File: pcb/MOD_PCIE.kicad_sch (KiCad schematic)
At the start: 8 parts, among them J7 2041262-1, SW2 SW_DIP_x01

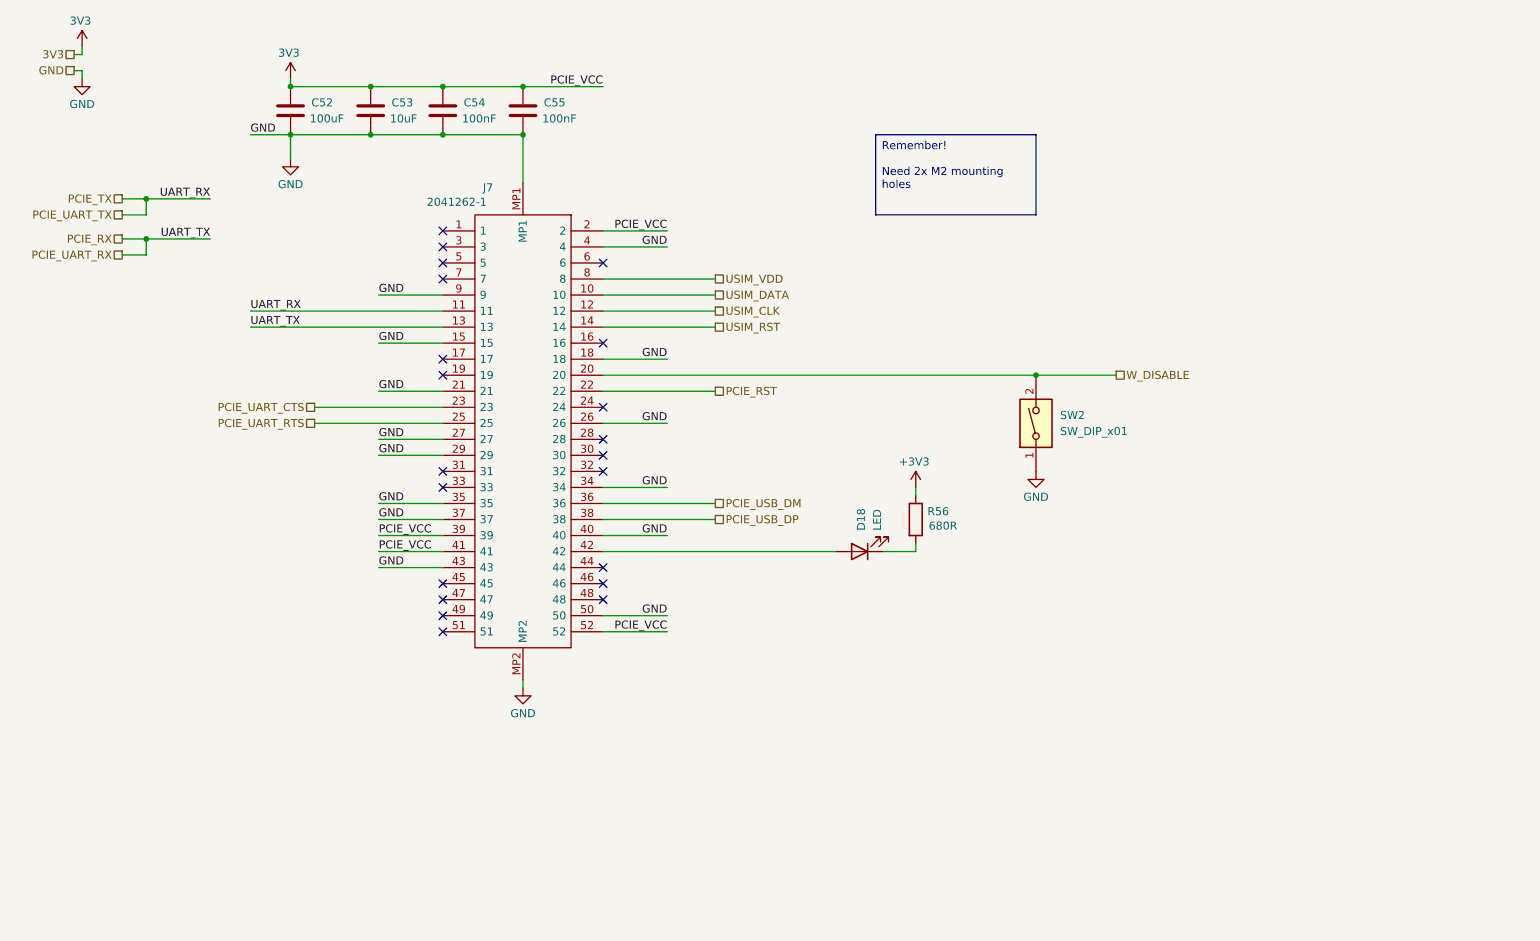
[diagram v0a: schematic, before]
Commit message: updated pcie sd and sim cards
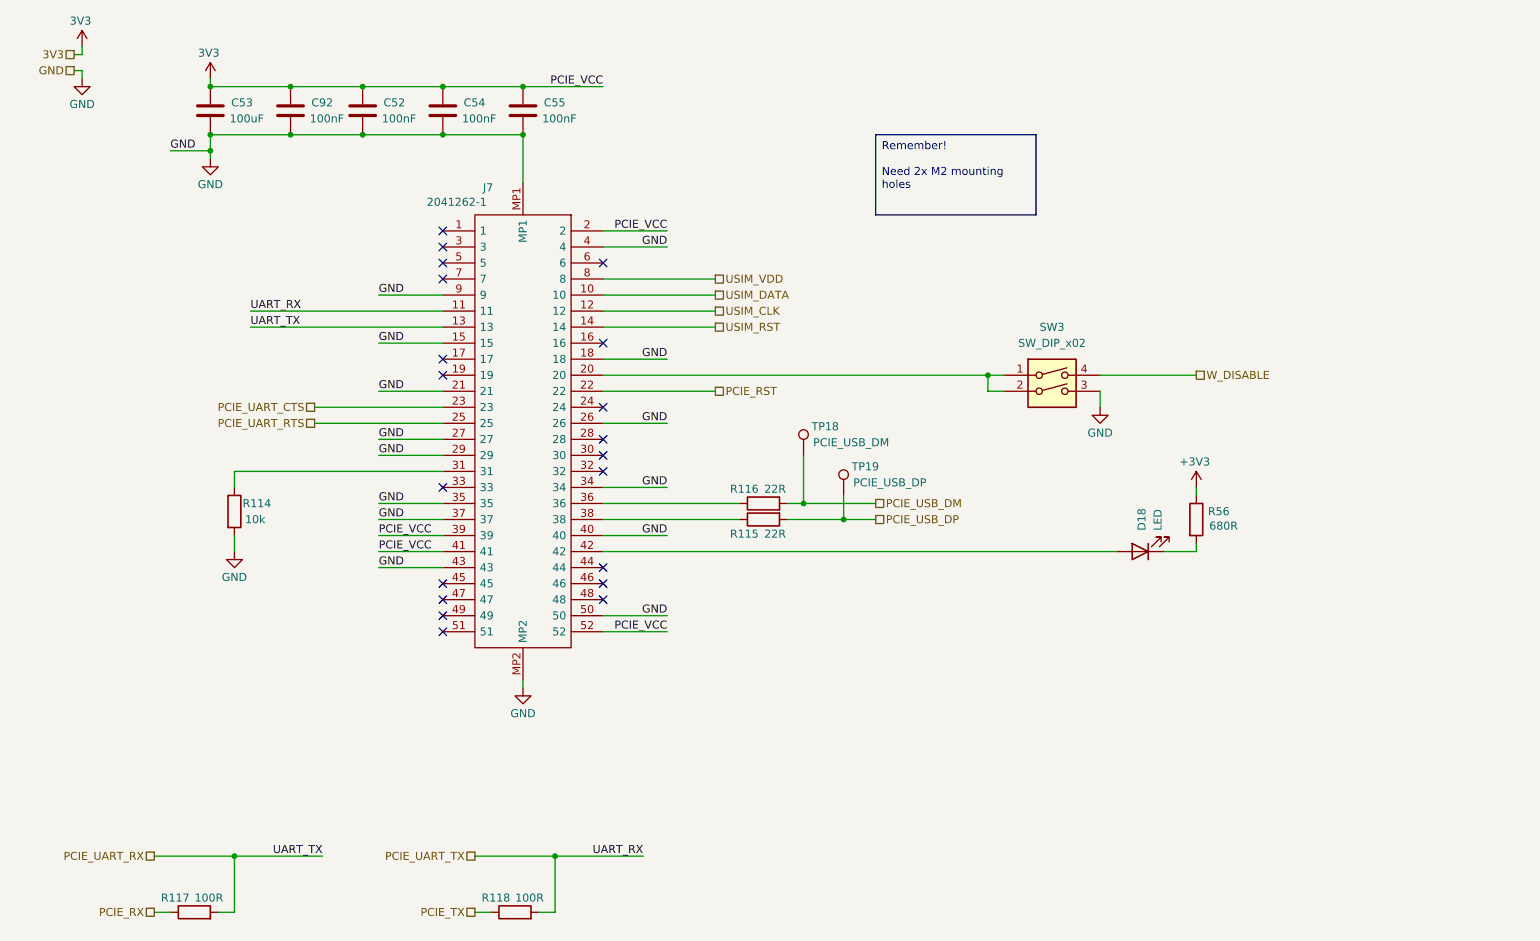
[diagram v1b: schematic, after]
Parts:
- removed SW2: SW_DIP_x01, SamacSys_Parts:DS01254L01BE, symbol Switch:SW_DIP_x01
- added C92: 100nF, Capacitor_SMD:C_0603_1608Metric_Pad1.08x0.95mm_HandSolder, symbol Device:C
- added R114: 10k, Resistor_SMD:R_0603_1608Metric_Pad0.98x0.95mm_HandSolder, symbol Device:R
- added R115, R116: 22R, Resistor_SMD:R_0603_1608Metric_Pad0.98x0.95mm_HandSolder, symbol Device:R
- added R117, R118: 100R, Resistor_SMD:R_0603_1608Metric_Pad0.98x0.95mm_HandSolder, symbol Device:R
- added SW3: SW_DIP_x02, symbol Switch:SW_DIP_x02
- added TP18: PCIE_USB_DM, TestPoint:TestPoint_THTPad_D2.0mm_Drill1.0mm, symbol Connector:TestPoint
- added TP19: PCIE_USB_DP, TestPoint:TestPoint_THTPad_D2.0mm_Drill1.0mm, symbol Connector:TestPoint
- C52: value 100uF -> 100nF; footprint Capacitor_SMD:C_1210_3225Metric_Pad1.33x2.70mm_HandSolder -> Capacitor_SMD:C_0603_1608Metric_Pad1.08x0.95mm_HandSolder
- C53: value 10uF -> 100uF; footprint Capacitor_SMD:C_0603_1608Metric_Pad1.08x0.95mm_HandSolder -> Capacitor_SMD:C_1210_3225Metric_Pad1.33x2.70mm_HandSolder
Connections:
- net 3V3: now also C92.1
- net GND: now also C92.2, R114.2, SW3.3
- net PCIE_RX: now also R117.1; no longer J7.13
- net PCIE_TX: now also R118.1; no longer J7.11
- net PCIE_USB_DM: now also R116.2, TP18.1; no longer J7.36
- net PCIE_USB_DP: now also R115.2, TP19.1; no longer J7.38
- net W_DISABLE: now also SW3.4; no longer J7.20
- net at J7.31: now also R114.1
- new net: J7.20, SW3.1, SW3.2
- new net: J7.36, R116.1
- new net: J7.38, R115.1
- new net PCIE_UART_RX: J7.13, R117.2
- new net PCIE_UART_TX: J7.11, R118.2
- no-connect marks 21 -> 20
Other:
- moved on the sheet: C53, D18, R56

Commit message: reannotated, updated some symbols
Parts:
- removed SW3: SW_DIP_x02, symbol Switch:SW_DIP_x02
- added S5: 2454985-2, 24549852, symbol 0_SamacSys_Parts:2454985-2
- renumbered C53 to C58, C92 to C59, C52 to C60, C54 to C61, C55 to C62, D18 to D20, R117 to R72, R114 to R73, R118 to R76, R116 to R78, R115 to R79, R56 to R80, TP18 to TP12, TP19 to TP13
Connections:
- net GND: now also S5.A2 (2)
- net W_DISABLE: now also S5.B2 (4)
- net at J7.20: now also S5.A1 (1), S5.B1 (3)

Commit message: minor changes before layout
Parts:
- removed R78, R79: 22R, Resistor_SMD:R_0603_1608Metric_Pad0.98x0.95mm_HandSolder, symbol Device:R
- removed TP12: PCIE_USB_DM, TestPoint:TestPoint_THTPad_D2.0mm_Drill1.0mm, symbol Connector:TestPoint
- removed TP13: PCIE_USB_DP, TestPoint:TestPoint_THTPad_D2.0mm_Drill1.0mm, symbol Connector:TestPoint
- added C94, C95: 47uF, Capacitor_SMD:C_0603_1608Metric_Pad1.08x0.95mm_HandSolder, symbol Device:C
- added TP23: PCIE_RX, TestPoint:TestPoint_THTPad_D2.0mm_Drill1.0mm, symbol Connector:TestPoint
- added TP24: PCIE_TX, TestPoint:TestPoint_THTPad_D2.0mm_Drill1.0mm, symbol Connector:TestPoint
- C58: value 100uF -> 47uF; footprint Capacitor_SMD:C_1210_3225Metric_Pad1.33x2.70mm_HandSolder -> Capacitor_SMD:C_0603_1608Metric_Pad1.08x0.95mm_HandSolder
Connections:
- net 3V3: now also C94.1, C95.1
- net GND: now also C94.2, C95.2
- net PCIE_UART_RX: now also TP23.1
- net PCIE_UART_TX: now also TP24.1
- net PCIE_USB_DM: now also J7.36
- net PCIE_USB_DP: now also J7.38
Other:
- moved on the sheet: C58, C59, C60, C61, C62, D20, J7, R73, R80, S5

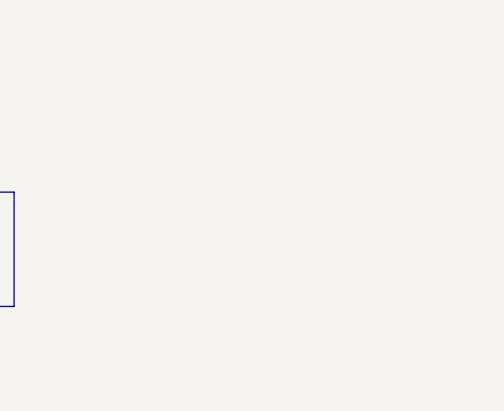
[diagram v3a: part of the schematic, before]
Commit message: initial layout of pcb with connectors, wlan and pcie modules
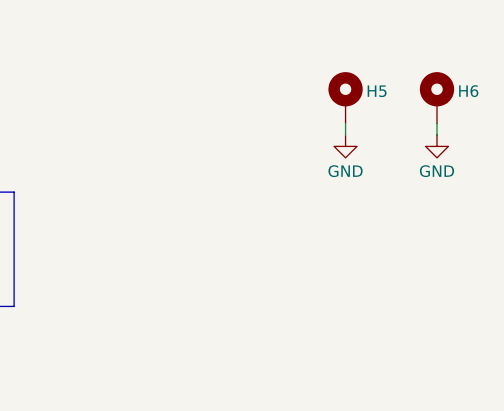
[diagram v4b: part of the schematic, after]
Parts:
- added H5, H6: MountingHole_Pad, MountingHole:MountingHole_2.7mm_M2.5_Pad, symbol Mechanical:MountingHole_Pad
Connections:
- net GND: now also H5.1, H6.1

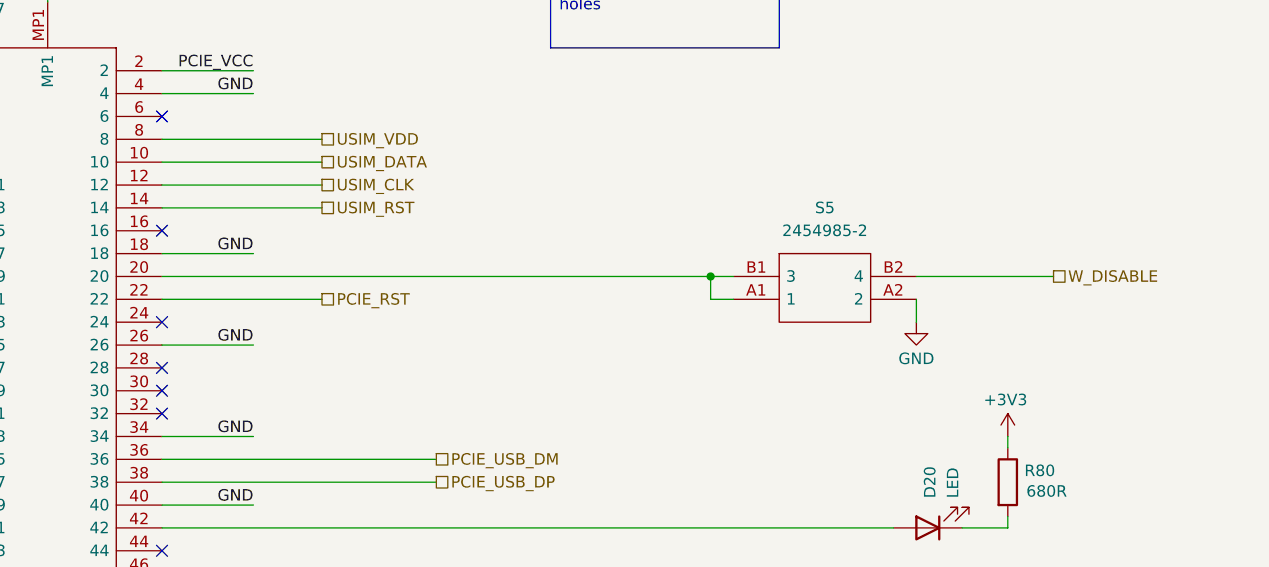
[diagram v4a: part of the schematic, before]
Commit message: laid out most of esp
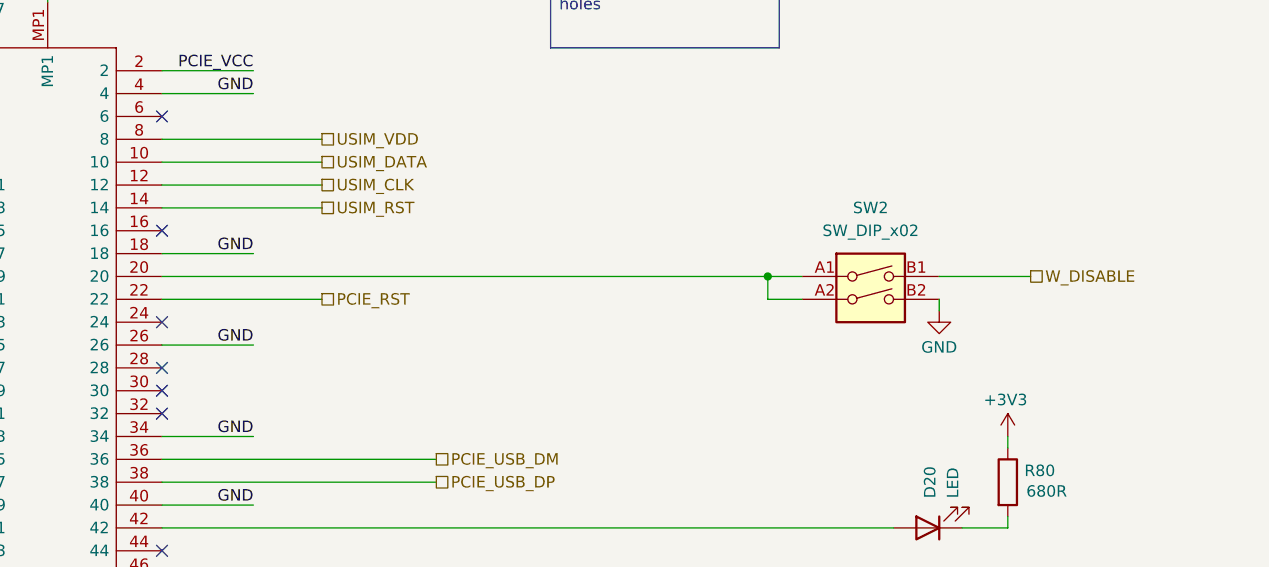
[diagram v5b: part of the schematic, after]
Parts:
- removed S5: 2454985-2, 24549852, symbol 0_SamacSys_Parts:2454985-2
- added SW2: SW_DIP_x02, SamacSys_Parts:EDS02SNRNTR04Q, symbol Switch:SW_DIP_x02
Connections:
- net GND: now also SW2.B2
- net W_DISABLE: now also SW2.B1
- net at J7.20: now also SW2.A1, SW2.A2
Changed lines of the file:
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@@
+	)
+	(junction
+		(at 201.93 76.2)
+		(diameter 0)
+		(color 0 0 0 0)
 	)
 	(junction
@@
 		(color 0 0 0 0)
 	)
-	(junction
-		(at 195.58 76.2)
-		(diameter 0)
-		(color 0 0 0 0)
-	)
 	(no_connect
 		(at 109.22 58.42)
@@
 	(wire
 		(pts
+			(xy 201.93 78.74) (xy 201.93 76.2)
+		)
+		(stroke
+			(width 0)
+			(type default)
+		)
+	)
+	(wire
+		(pts
+			(xy 220.98 76.2) (xy 231.14 76.2)
+		)
+		(stroke
+			(width 0)
+			(type default)
+		)
+	)
+	(wire
+		(pts
 			(xy 73.66 38.1) (xy 85.09 38.1)
 		)
@@
 	(wire
 		(pts
-			(xy 195.58 76.2) (xy 198.12 76.2)
-		)
-		(stroke
-			(width 0)
-			(type default)
-		)
-	)
-	(wire
-		(pts
 			(xy 73.66 30.48) (xy 85.09 30.48)
 		)
@@
 	(wire
 		(pts
-			(xy 195.58 78.74) (xy 195.58 76.2)
-		)
-		(stroke
-			(width 0)
-			(type default)
-		)
-	)
-	(wire
-		(pts
 			(xy 96.52 38.1) (xy 109.22 38.1)
 		)
@@
 	(wire
 		(pts
-			(xy 134.62 76.2) (xy 195.58 76.2)
+			(xy 134.62 76.2) (xy 201.93 76.2)
 		)
 		(stroke
@@
 	(wire
 		(pts
-			(xy 218.44 76.2) (xy 233.68 76.2)
-		)
-		(stroke
-			(width 0)
-			(type default)
-		)
-	)
-	(wire
-		(pts
 			(xy 134.62 78.74) (xy 152.4 78.74)
 		)
@@
 	(wire
 		(pts
-			(xy 198.12 78.74) (xy 195.58 78.74)
-		)
-		(stroke
-			(width 0)
-			(type default)
-		)
-	)
-	(wire
-		(pts
 			(xy 240.03 30.48) (xy 240.03 31.75)
 		)
@@
 	(wire
 		(pts
-			(xy 218.44 78.74) (xy 218.44 81.28)
-		)
-		(stroke
-			(width 0)
-			(type default)
-		)
-	)
-	(wire
-		(pts
 			(xy 152.4 68.58) (xy 134.62 68.58)
 		)
@@
 	(wire
 		(pts
+			(xy 201.93 76.2) (xy 205.74 76.2)
+		)
+		(stroke
+			(width 0)
+			(type default)
+		)
+	)
+	(wire
+		(pts
 			(xy 50.8 38.1) (xy 62.23 38.1)
 		)
@@
 	(wire
 		(pts
+			(xy 205.74 78.74) (xy 201.93 78.74)
+		)
+		(stroke
+			(width 0)
+			(type default)
+		)
+	)
+	(wire
+		(pts
 			(xy 228.6 93.98) (xy 228.6 95.25)
 		)
@@
 		(pts
 			(xy 96.52 30.48) (xy 109.22 30.48)
+		)
+		(stroke
+			(width 0)
+			(type default)
+		)
+	)
+	(wire
+		(pts
+			(xy 220.98 78.74) (xy 220.98 80.01)
 		)
 		(stroke
@@
 	(hierarchical_label "W_DISABLE"
 		(shape passive)
-		(at 233.68 76.2 0)
+		(at 231.14 76.2 0)
 		(effects
 			(font
@@
 	)
 	(symbol
-		(lib_id "0_SamacSys_Parts:2454985-2")
-		(at 198.12 76.2 0)
-		(unit 1)
-		(exclude_from_sim no)
-		(in_bom yes)
-		(on_board yes)
-		(dnp no)
-		(fields_autoplaced yes)
-		(property "Reference" "S5"
-			(at 208.28 68.58 0)
-			(effects
-				(font
-					(size 1.27 1.27)
-				)
-			)
-		)
-		(property "Value" "2454985-2"
-			(at 208.28 71.12 0)
-			(effects
-				(font
-					(size 1.27 1.27)
-				)
-			)
-		)
-		(property "Footprint" "24549852"
-			(at 214.63 73.66 0)
-			(effects
-				(font
-					(size 1.27 1.27)
-				)
-				(justify left)
-				(hide yes)
-			)
-		)
-		(property "Datasheet" "https://www.te.com/commerce/DocumentDelivery/DDEController?Action=showdoc&DocId=Customer+Drawing%7F2454985%7F1%7Fpdf%7FEnglish%7FENG_CD_2454985_1.pdf%7F2454985-2"
-			(at 214.63 76.2 0)
-			(effects
-				(font
-					(size 1.27 1.27)
-				)
-				(justify left)
-				(hide yes)
-			)
-		)
-		(property "Description" "DIP & SIP Switches, Gold Flash, Black, PA9T, 2 Switch, -40  85 C, DIP, Extended Actuator Style, 24A Contact Current Rating, Alcoswitch DIP ADE"
-			(at 198.12 76.2 0)
-			(effects
-				(font
-					(size 1.27 1.27)
-				)
-				(hide yes)
-			)
-		)
-		(property "Description_1" "DIP & SIP Switches, Gold Flash, Black, PA9T, 2 Switch, -40  85 C, DIP, Extended Actuator Style, 24A Contact Current Rating, Alcoswitch DIP ADE"
-			(at 214.63 78.74 0)
-			(effects
-				(font
-					(size 1.27 1.27)
-				)
-				(justify left)
-				(hide yes)
-			)
-		)
-		(property "Height" "4.85"
-			(at 214.63 81.28 0)
-			(effects
-				(font
-					(size 1.27 1.27)
-				)
-				(justify left)
-				(hide yes)
-			)
-		)
-		(property "Mouser Part Number" "655-2454985-2"
-			(at 214.63 83.82 0)
-			(effects
-				(font
-					(size 1.27 1.27)
-				)
-				(justify left)
-				(hide yes)
-			)
-		)
-		(property "Mouser Price/Stock" "https://www.mouser.co.uk/ProductDetail/TE-Connectivity-Alcoswitch/2454985-2?qs=1Kr7Jg1SGW9BJVCnMGNqBQ%3D%3D"
-			(at 214.63 86.36 0)
-			(effects
-				(font
-					(size 1.27 1.27)
-				)
-				(justify left)
-				(hide yes)
-			)
-		)
-		(property "Manufacturer_Name" "TE Connectivity"
-			(at 214.63 88.9 0)
-			(effects
-				(font
-					(size 1.27 1.27)
-				)
-				(justify left)
-				(hide yes)
-			)
-		)
-		(property "Manufacturer_Part_Number" "2454985-2"
-			(at 214.63 91.44 0)
-			(effects
-				(font
-					(size 1.27 1.27)
-				)
-				(justify left)
-				(hide yes)
-			)
-		)
-		(pin "A1"
-		)
-		(pin "A2"
-		)
-		(pin "B2"
-		)
-		(pin "B1"
-		)
-		(instances
-			(project ""
-				(path "/3aee14c3-5480-4f7c-989e-3fef81779034/77f505d1-5a70-4b67-92f2-4570e0aae5e4"
-					(reference "S5")
-					(unit 1)
-				)
-			)
-		)
-	)
-	(symbol
 		(lib_id "Device:C")
 		(at 73.66 34.29 0)
@@
 	(symbol
 		(lib_id "power:GND")
-		(at 218.44 81.28 0)
+		(at 220.98 80.01 0)
 		(mirror y)
 		(unit 1)
@@
 		(dnp no)
 		(property "Reference" "#PWR0304"
-			(at 218.44 87.63 0)
+			(at 220.98 86.36 0)
 			(effects
 				(font
@@
 		)
 		(property "Value" "GND"
-			(at 218.44 85.344 0)
+			(at 220.98 84.074 0)
 			(effects
 				(font
@@
 		)
 		(property "Footprint" ""
-			(at 218.44 81.28 0)
+			(at 220.98 80.01 0)
 			(effects
 				(font
@@
 		)
 		(property "Datasheet" ""
-			(at 218.44 81.28 0)
+			(at 220.98 80.01 0)
 			(effects
 				(font
@@
 		)
 		(property "Description" "Power symbol creates a global label with name \"GND\" , ground"
-			(at 218.44 81.28 0)
+			(at 220.98 80.01 0)
 			(effects
 				(font
@@
 					(unit 1)
 				)
+			)
+		)
+	)
+	(symbol
+		(lib_id "Switch:SW_DIP_x02")
+		(at 213.36 78.74 0)
+		(unit 1)
+		(exclude_from_sim no)
+		(in_bom yes)
+		(on_board yes)
+		(dnp no)
+		(fields_autoplaced yes)
+		(property "Reference" "SW2"
+			(at 213.36 68.58 0)
+			(effects
+				(font
+					(size 1.27 1.27)
+				)
+			)
+		)
+		(property "Value" "SW_DIP_x02"
+			(at 213.36 71.12 0)
+			(effects
+				(font
+					(size 1.27 1.27)
+				)
+			)
+		)
+		(property "Footprint" "SamacSys_Parts:EDS02SNRNTR04Q"
+			(at 213.36 78.74 0)
+			(effects
+				(font
+					(size 1.27 1.27)
+				)
+				(hide yes)
+			)
+		)
+		(property "Datasheet" "~"
+			(at 213.36 78.74 0)
+			(effects
+				(font
+					(size 1.27 1.27)
+				)
+				(hide yes)
+			)
+		)
+		(property "Description" "2x DIP Switch, Single Pole Single Throw (SPST) switch, small symbol"
+			(at 213.36 78.74 0)
+			(effects
+				(font
+					(size 1.27 1.27)
+				)
+				(hide yes)
+			)
+		)
+		(pin "A1"
+		)
+		(pin "B2"
+		)
+		(pin "A2"
+		)
+		(pin "B1"
+		)
+		(instances
+			(project ""
+				(path "/3aee14c3-5480-4f7c-989e-3fef81779034/77f505d1-5a70-4b67-92f2-4570e0aae5e4"
+					(reference "SW2")
+					(unit 1)
+				)
